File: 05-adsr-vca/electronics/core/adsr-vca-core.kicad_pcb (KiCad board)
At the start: 2 copper layers, 58 x 65 mm, 70 parts, among them J2 Conn_02x03_Odd_Even, J3 Conn_02x03_Odd_Even, J4 Conn_02x06_Odd_Even, J5 Conn_02x03_Odd_Even, J6 Conn_01x02, J7 Conn_02x05_Odd_Even, J8 Conn_02x03_Odd_Even, Q1 BC857, Q2 BC847, Q3 BC847BS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

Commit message: ADSR PCB's production ready
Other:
- board text added: "GATD"
- board text added: "GATI"
- board text added: "VCIN"
- board text added: "VCOU"
- board text added: "VCOUT"
- board text removed: "NC"
- board text removed: "VIN"
- board text removed: "VOUT"
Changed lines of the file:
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@@
-		)
-	)
-	(gr_text "ENV"
-		(at 145.59 44.127 180)
-		(layer "F.SilkS")
-		(effects
-			(font
-				(size 1 0.75)
-				(thickness 0.15)
-				(bold yes)
-			)
-			(justify bottom)
 		)
 	)
@@
 		)
 	)
-	(gr_text "VOUT"
-		(at 153.21 44.127 180)
-		(layer "F.SilkS")
-		(effects
-			(font
-				(size 1 0.75)
-				(thickness 0.15)
-				(bold yes)
-			)
-			(justify bottom)
-		)
-	)
-	(gr_text "NC"
+	(gr_text "VCOUT"
 		(at 155.877 44.127 180)
 		(layer "F.SilkS")
@@
 			(font
 				(size 1 0.75)
-				(thickness 0.15)
+				(thickness 0.17)
 				(bold yes)
 			)
@@
 		)
 	)
-	(gr_text "GATE"
-		(at 143.05 44.127 180)
-		(layer "F.SilkS")
-		(effects
-			(font
-				(size 1 0.75)
-				(thickness 0.15)
+	(gr_text "VCIN"
+		(at 150.162 44.127 180)
+		(layer "F.SilkS")
+		(effects
+			(font
+				(size 1 0.75)
+				(thickness 0.17)
+				(bold yes)
+			)
+			(justify bottom)
+		)
+	)
+	(gr_text "ENV"
+		(at 147.622 44.127 180)
+		(layer "F.SilkS")
+		(effects
+			(font
+				(size 1 0.75)
+				(thickness 0.17)
 				(bold yes)
 			)
@@
 		)
 	)
+	(gr_text "GATI"
+		(at 145.082 44.127 180)
+		(layer "F.SilkS")
+		(effects
+			(font
+				(size 1 0.75)
+				(thickness 0.17)
+				(bold yes)
+			)
+			(justify bottom)
+		)
+	)
 	(gr_text "A1"
 		(at 133.017 99.118 0)
@@
 		)
 	)
-	(gr_text "VIN"
-		(at 148.003 44.127 180)
-		(layer "F.SilkS")
-		(effects
-			(font
-				(size 1 0.75)
-				(thickness 0.15)
-				(bold yes)
-			)
-			(justify bottom)
-		)
-	)
 	(gr_text "VCV"
-		(at 150.675 44.127 180)
-		(layer "F.SilkS")
-		(effects
-			(font
-				(size 1 0.75)
-				(thickness 0.15)
+		(at 152.702 44.127 180)
+		(layer "F.SilkS")
+		(effects
+			(font
+				(size 1 0.75)
+				(thickness 0.17)
 				(bold yes)
 			)
@@
 		)
 	)
+	(gr_text "GATD"
+		(at 142.288 44.127 180)
+		(layer "F.SilkS")
+		(effects
+			(font
+				(size 1 0.75)
+				(thickness 0.17)
+				(bold yes)
+			)
+			(justify bottom)
+		)
+	)
 	(gr_text "ENV"
 		(at 133.017 96.578 0)
@@
 		)
 	)
-	(gr_text "VOUT"
-		(at 153.21 44.127 180)
+	(gr_text "VCOU"
+		(at 156.004 44.127 180)
 		(layer "B.SilkS")
 		(effects
@@
 		)
 	)
-	(gr_text "NC"
-		(at 155.877 44.127 180)
+	(gr_text "ENV"
+		(at 148.003 44.127 180)
+		(layer "B.SilkS")
+		(effects
+			(font
+				(size 1 0.75)
+				(thickness 0.15)
+				(bold yes)
+			)
+			(justify bottom mirror)
+		)
+	)
+	(gr_text "VCV"
+		(at 153.21 44.127 180)
 		(layer "B.SilkS")
 		(effects
@@
 		)
 	)
-	(gr_text "VCV"
+	(gr_text "VCIN"
 		(at 150.543 44.127 180)
 		(layer "B.SilkS")
@@
 		)
 	)
+	(gr_text "GATI"
+		(at 145.463 44.127 180)
+		(layer "B.SilkS")
+		(effects
+			(font
+				(size 1 0.75)
+				(thickness 0.15)
+				(bold yes)
+			)
+			(justify bottom mirror)
+		)
+	)
 	(gr_text "12V"
 		(at 151.6225 105.214 180)
-		(layer "B.SilkS")
-		(effects
-			(font
-				(size 1 0.75)
-				(thickness 0.15)
-				(bold yes)
-			)
-			(justify bottom mirror)
-		)
-	)
-	(gr_text "VIN"
-		(at 148.003 44.127 180)
 		(layer "B.SilkS")
 		(effects
@@
 		)
 	)
-	(gr_text "GATE"
+	(gr_text "GATD"
 		(at 142.796 44.127 180)
 		(layer "B.SilkS")
 		(effects
-			(font
-				(size 1 0.75)
-				(thickness 0.15)
-				(bold yes)
-			)
-			(justify bottom mirror)
-		)
-	)
-	(gr_text "ENV"
-		(at 145.463 44.127 180)
-		(layer "B.SilkS")
-		(effects

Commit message: ADSR production ready - round 2
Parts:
- removed the G*** at (136.3, 103.6)
- added R29: 200k, Resistor_SMD:R_0603_1608Metric, F.Cu at (144.8, 95.9)
- added RV_VCA_BIAS1: 100k, Potentiometer_THT:Potentiometer_ACP_CA6-H2,5_Horizontal, F.Cu at (137.0, 106.5)
- moved R23 3.22 mm to (144.8, 92.6)
- moved R21 2.36 mm to (146.4, 95.9), turned to 90 degrees
- moved C7 0.94 mm to (148.1, 95.9), turned to 90 degrees
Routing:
- net +12V: track 167.8 -> 182.3 mm, vias 0 -> 1
- net Net-(R29-Pad1): track 0.00 -> 13.0 mm, vias 0 -> 2
- net -12V: track 160.4 -> 167.9 mm
- net Net-(U2A--): track 6.46 -> 11.3 mm
- net Net-(Q3A-E1): track 13.2 -> 10.4 mm
- net GND: vias 340 -> 321
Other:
- board text added: "VCA BIAS"

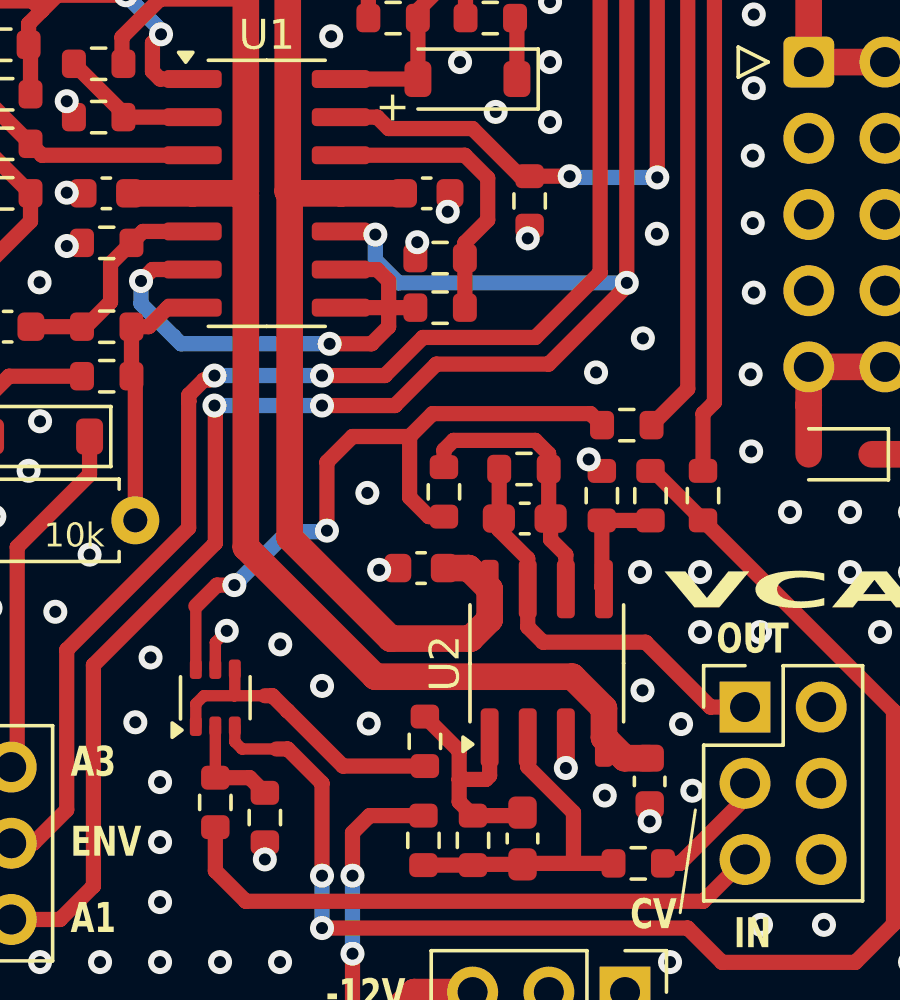
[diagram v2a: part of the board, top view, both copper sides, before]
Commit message: ADSR + VCA v0.2
- The + and - power pins on the VCA op-amp was accidentally swapped. This version fixes it
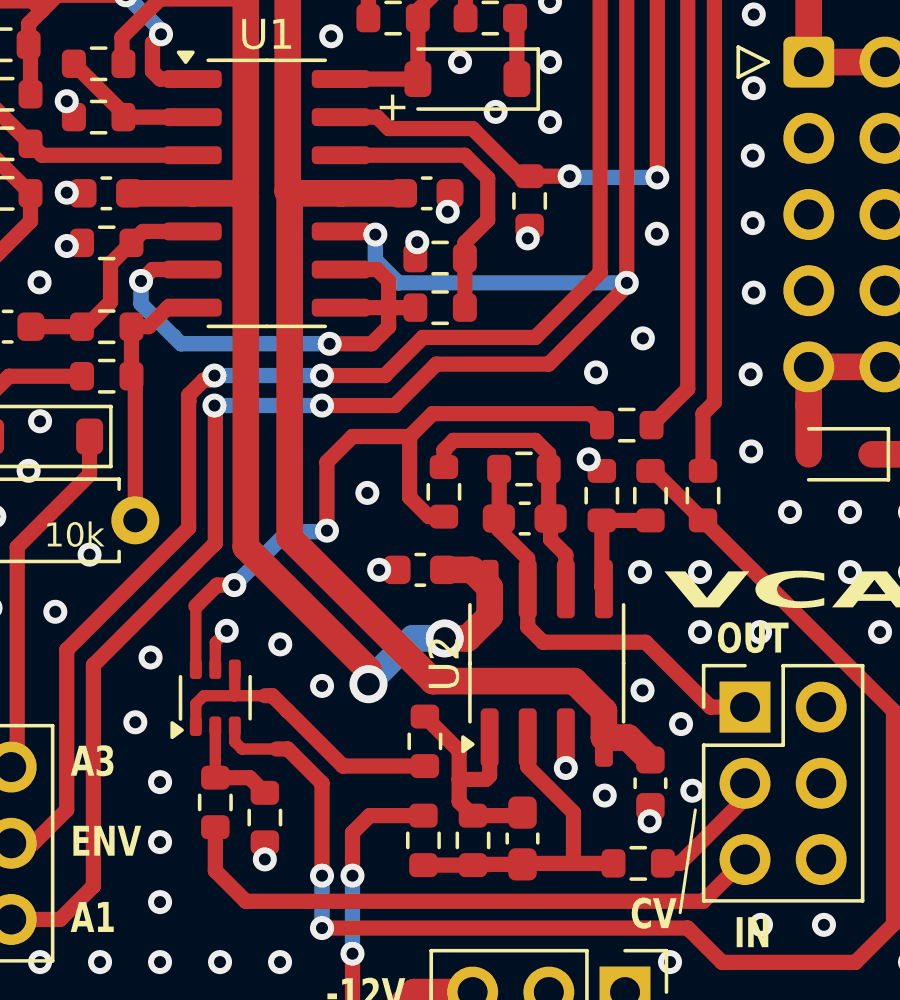
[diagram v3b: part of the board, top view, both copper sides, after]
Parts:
- moved C6 10.5 mm to (152.3, 94.0), turned to 90 degrees
- moved C5 10.4 mm to (144.7, 86.9), turned to 180 degrees
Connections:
- U2 pad 4: +12V -> -12V
- U2 pad 8: -12V -> +12V
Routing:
- net -12V: track 167.9 -> 172.4 mm
- net +12V: track 182.3 -> 179.3 mm, vias 1 -> 3
- net GND: vias 321 -> 320
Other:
- board text added: "HM-05 ADSR VCA V0.2 / 2025 Aug"
- board text removed: "HM-05 ADSR VCA V0.1 / 2025 Aug"

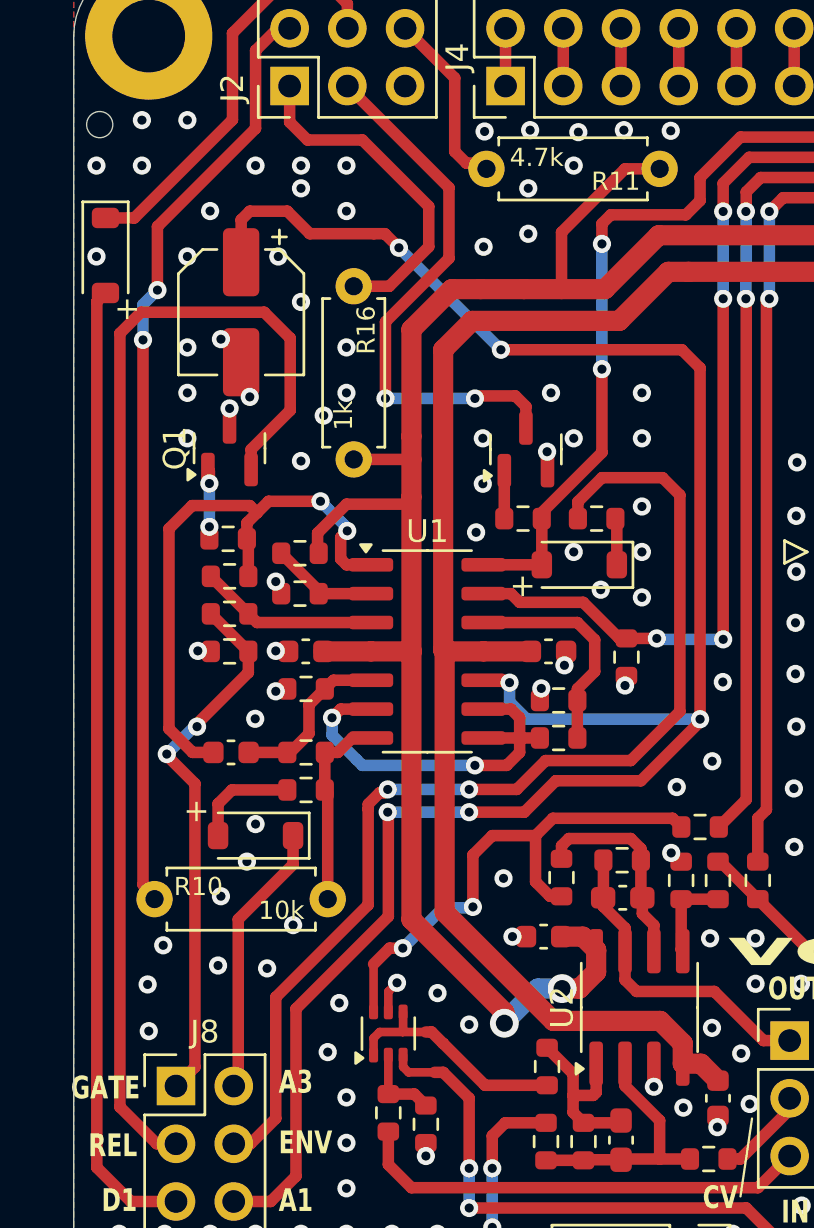
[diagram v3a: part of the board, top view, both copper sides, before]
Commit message: Replaced THT comps. to SMD on ADSR/VCA
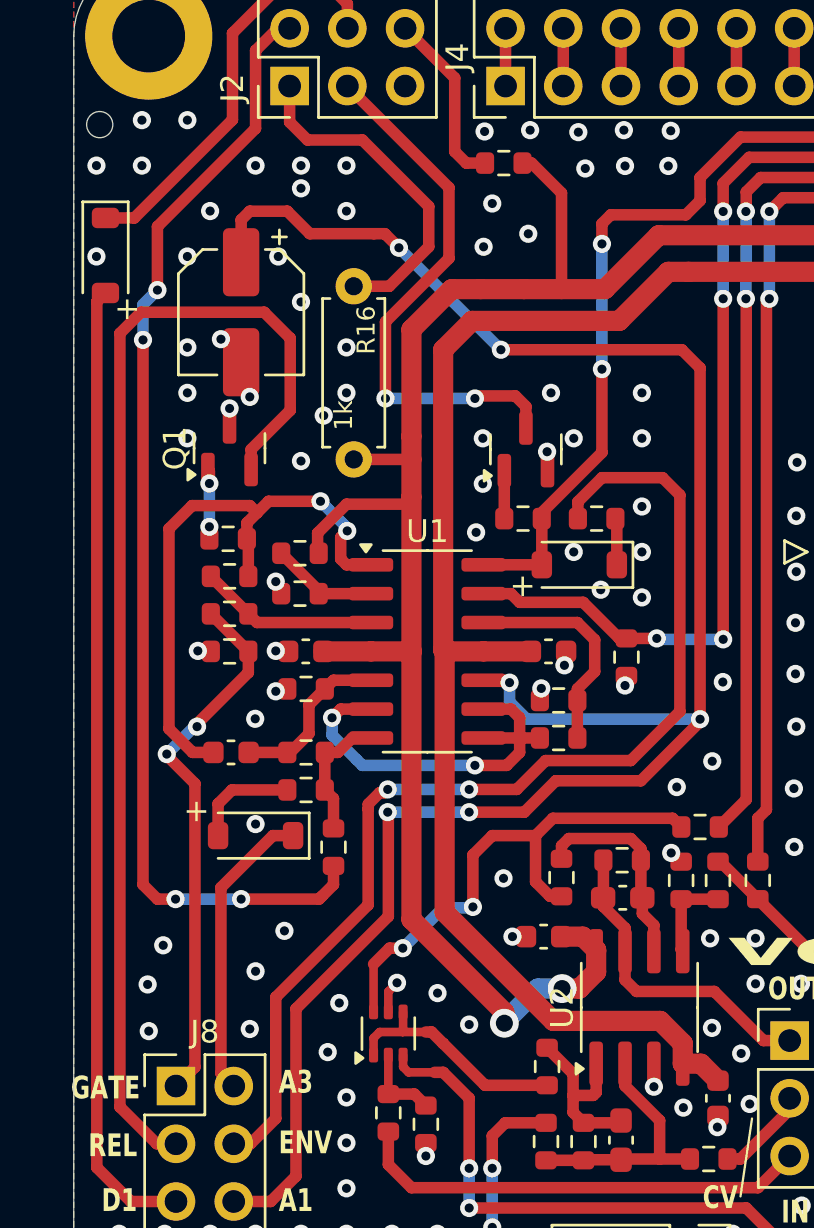
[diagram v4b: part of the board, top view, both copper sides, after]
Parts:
- R10, R11: footprint Shmoergh_Custom_Footprints:R_Axial_DIN0207_L6.3mm_D2.5mm_P7.62mm_Horizontal -> Resistor_SMD:R_0603_1608Metric
- moved R10 8.20 mm to (135.4, 83.0), turned to -90 degrees
- moved R11 6.86 mm to (142.9, 52.9), turned to 0 degrees
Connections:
- R10 pad 1: SUSTAIN_1 -> Net-(R10-Pad1)
- R10 pad 2: Net-(R10-Pad2) -> SUSTAIN_1
- R11 pad 1: +12V -> SUSTAIN_3
- R11 pad 2: SUSTAIN_3 -> +12V
- R7 pad 1: Net-(R10-Pad2) -> Net-(R10-Pad1)
- R9 pad 2: Net-(R10-Pad2) -> Net-(R10-Pad1)
- U1 pad 7: Net-(R10-Pad2) -> Net-(R10-Pad1)
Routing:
- net SUSTAIN_1: track 41.5 -> 50.4 mm, vias 2 -> 4
- net Net-(R10-Pad2): track 8.81 -> 0.00 mm
- net Net-(R10-Pad1): track 0.00 -> 5.80 mm
- net +12V: track 179.3 -> 177.9 mm
- net ATTACK_3: track 12.1 -> 13.1 mm

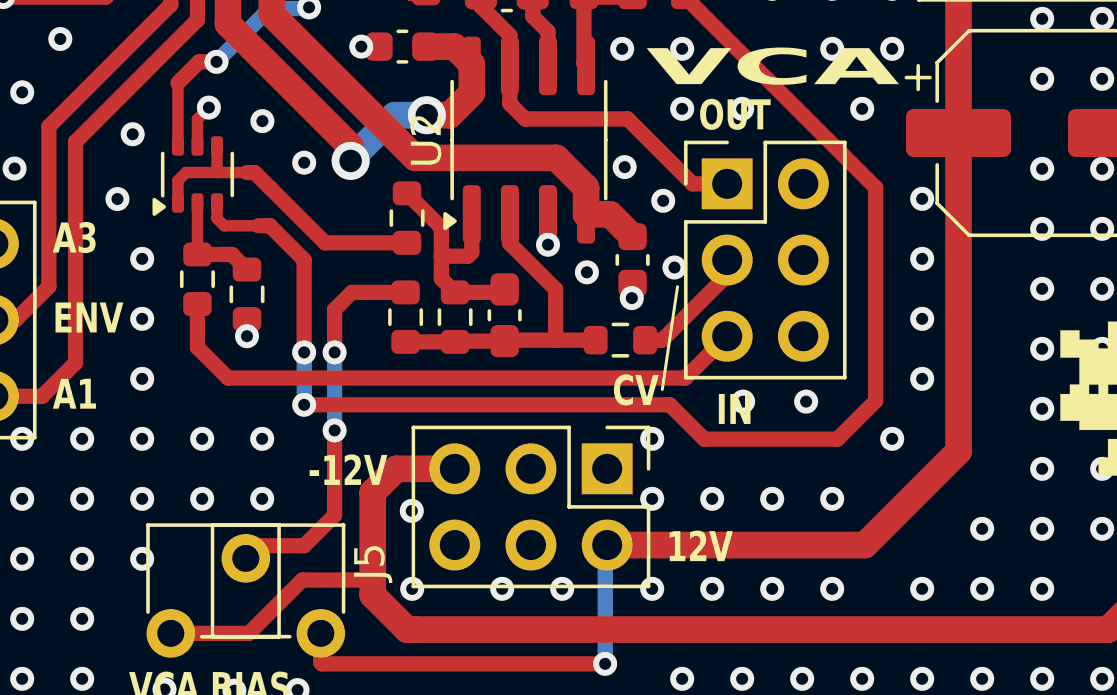
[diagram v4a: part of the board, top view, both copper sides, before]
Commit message: PSU v0.2 and fixed crosstalk on VCA
- added PSU v0.2
- VCA had a crosstalk issue. The input signal got superimposed on the output. The current solution is to move the input voltage divider on the core board as close to the input pin header connection as possible. Additionally, I added the 100k resistor as a THT component to the UI board. Only one of the 100k resistors is needed, but I added both for testing purposes.
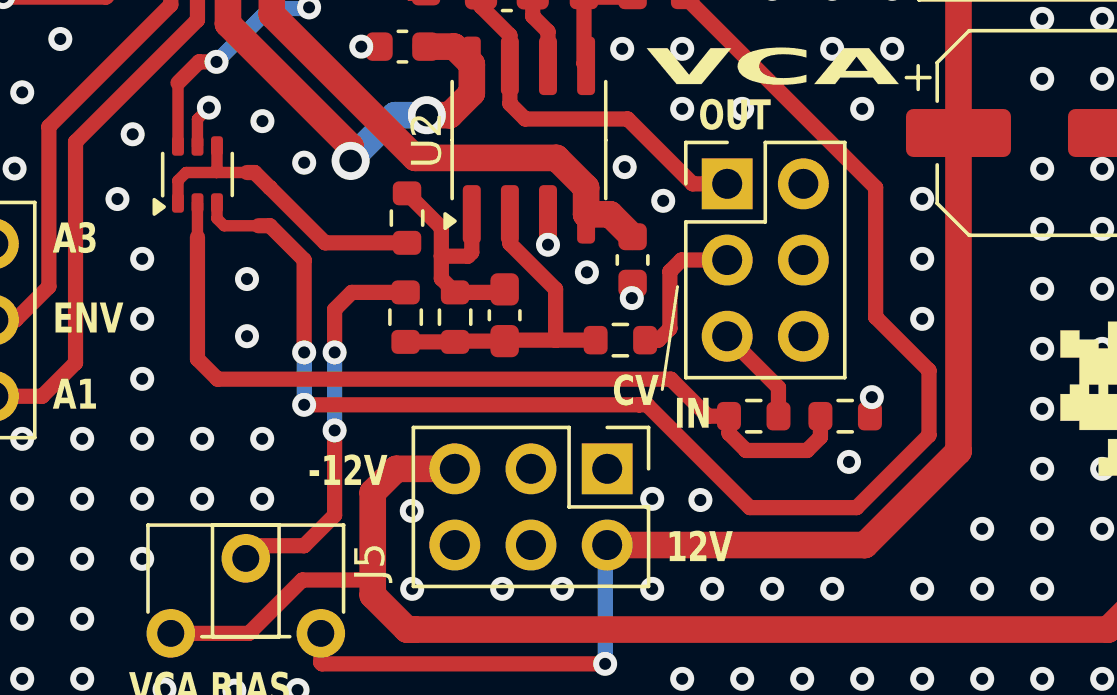
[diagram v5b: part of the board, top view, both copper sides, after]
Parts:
- moved R20 20.3 mm to (159.4, 99.2), turned to 180 degrees
- moved R18 19.1 mm to (156.4, 99.2), turned to 180 degrees
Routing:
- net Net-(Q3A-B1): track 3.57 -> 28.4 mm
- net VCA_IN: track 20.1 -> 3.37 mm
- net Net-(Q3B-C2): track 47.4 -> 52.5 mm
- net VCA_CV: track 4.14 -> 4.96 mm
- net GND: vias 320 -> 315

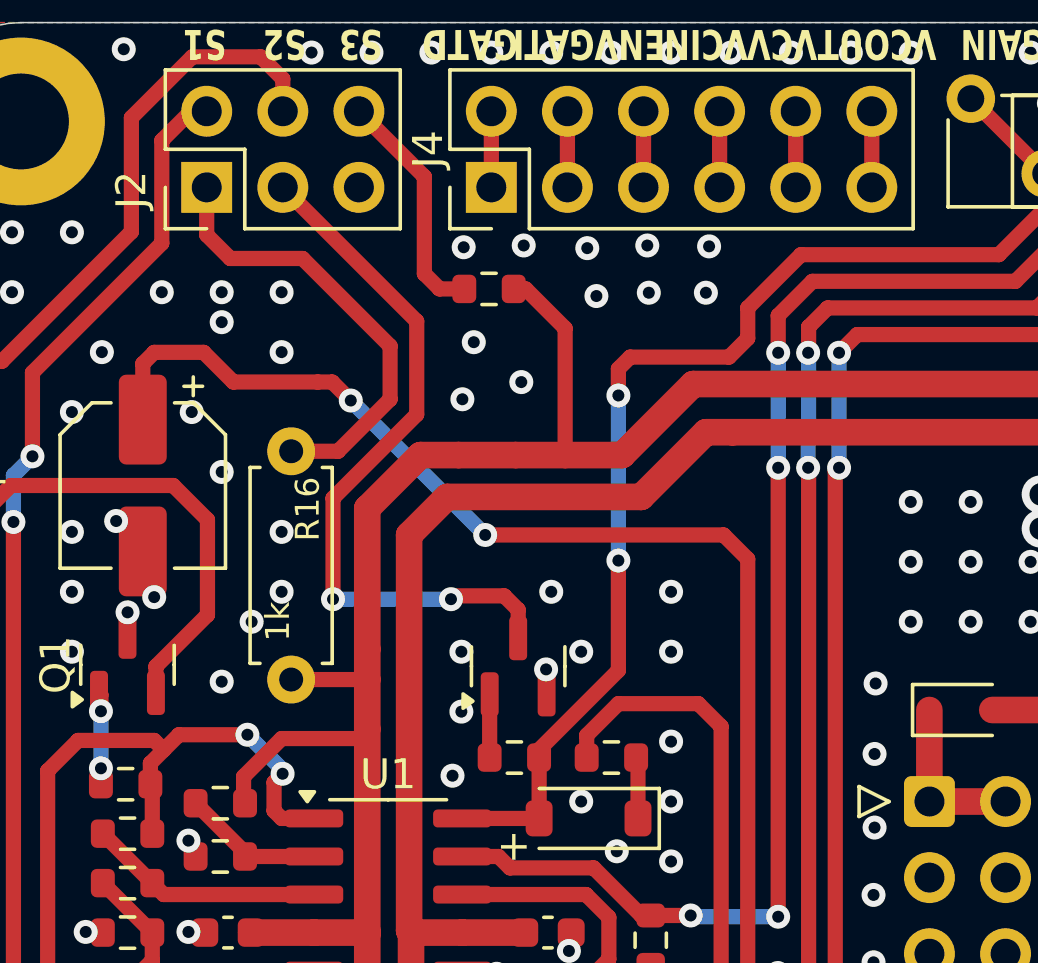
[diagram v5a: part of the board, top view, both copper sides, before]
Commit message: Moved LED from ADSR core to UI board
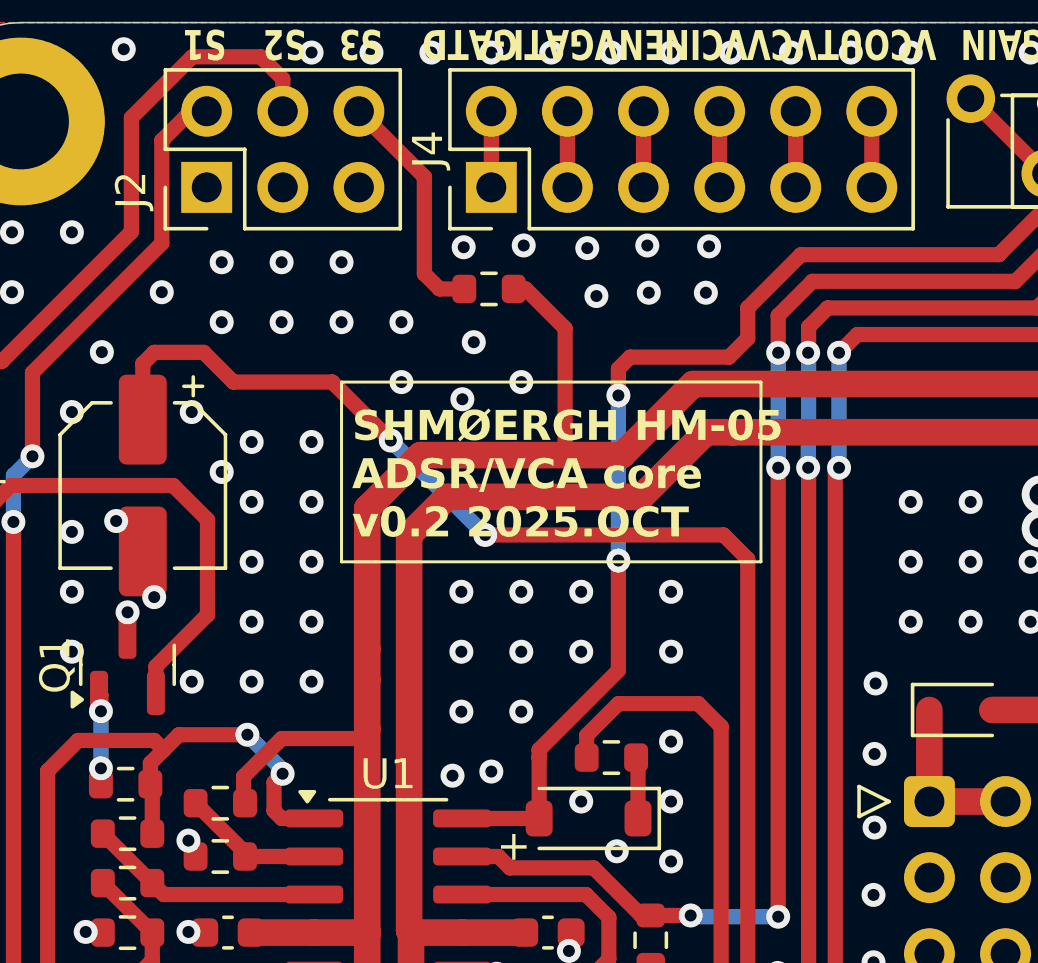
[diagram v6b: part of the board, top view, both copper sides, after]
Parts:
- removed Q2: BC847, Package_TO_SOT_SMD:SOT-23
- removed R15: 47k, Resistor_SMD:R_0603_1608Metric
- removed R16: 1k, Shmoergh_Custom_Footprints:R_Axial_DIN0207_L6.3mm_D2.5mm_P7.62mm_Horizontal
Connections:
- J2 pad 1: LED_A -> GND
- J2 pad 3: LED_K -> GND
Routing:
- net LED_K: track 24.2 -> 0.00 mm, vias 2 -> 0
- net LED_A: track 15.0 -> 0.00 mm
- net +12V: track 177.9 -> 175.3 mm
- net Net-(Q2-B): track 2.11 -> 0.00 mm
- net GND: track 1.35 -> 1.42 mm, vias 315 -> 330
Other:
- board text added: "SHMØERGH HM-05 ADSR/VCA core v0.2 2025.OCT"
